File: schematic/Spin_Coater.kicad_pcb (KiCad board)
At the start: 2 copper layers, 135 x 80 mm, 97 parts, among them J1 USB_C_Receptacle_USB2.0_14P, J2 Motor Encoder In, J3 USB_B_Micro, M1A TestPoint, M1B TestPoint, M1C TestPoint, Q1 AONR21357, Q2 GSFN6982, Q3 GSFN6982, Q4 GSFN6982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

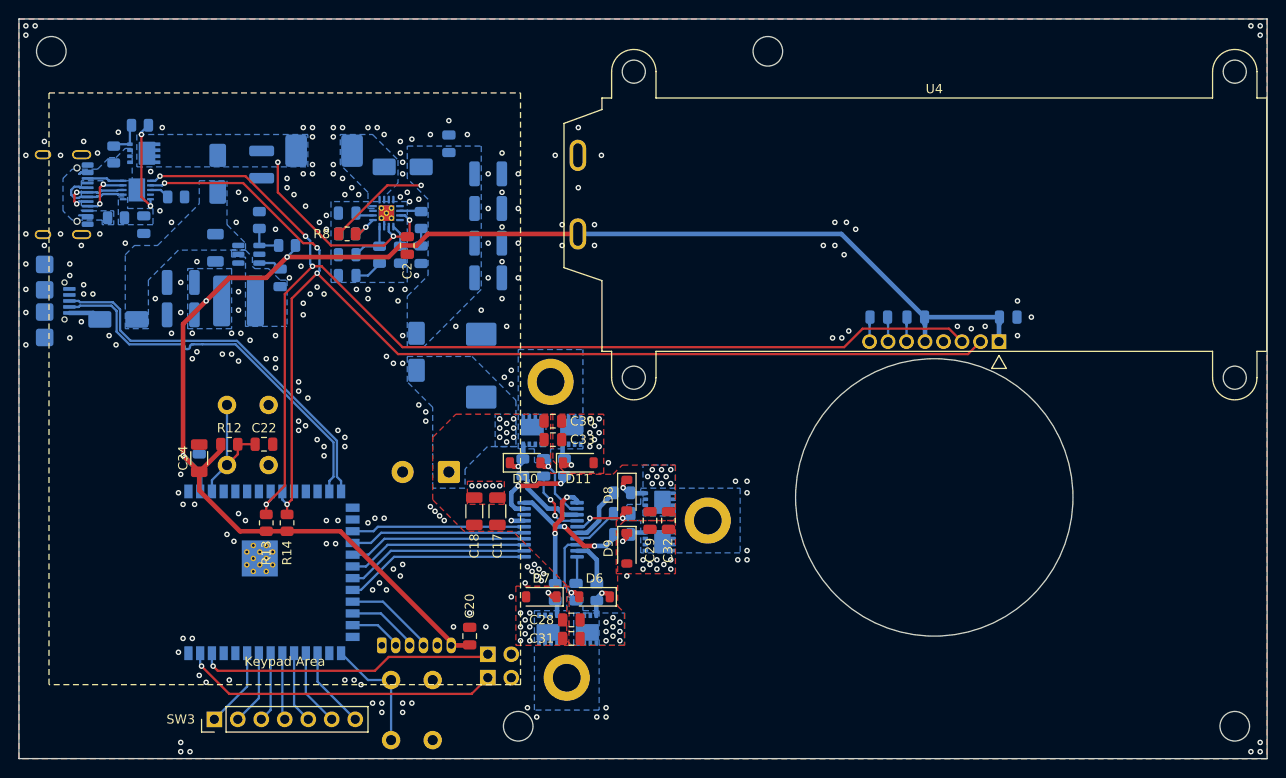
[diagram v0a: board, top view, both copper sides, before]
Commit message: Added button debouncing
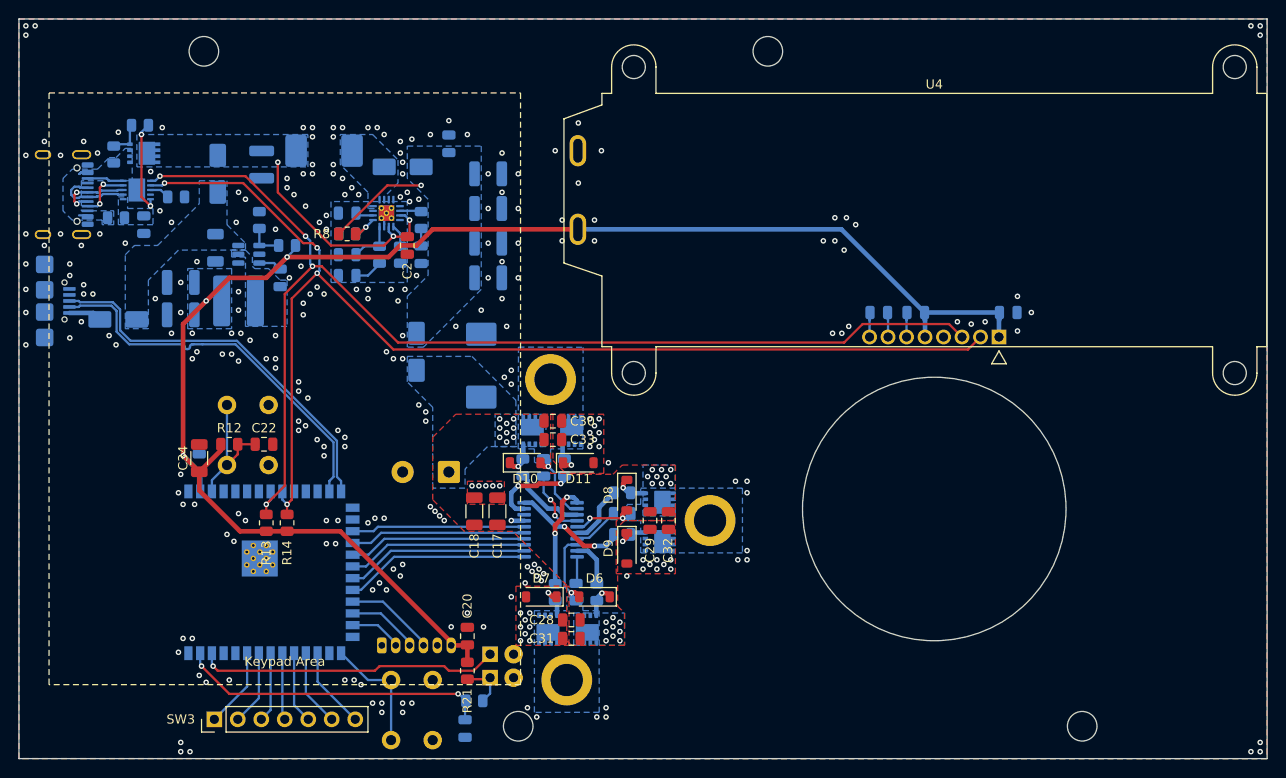
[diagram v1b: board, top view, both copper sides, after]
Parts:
- added C36: 1uF, Capacitor_SMD:C_0805_2012Metric, B.Cu at (120.8, 146.8)
- added R21: 10k, Resistor_SMD:R_0805_2012Metric, F.Cu at (121.0, 140.5)
- added R22: 10k, Resistor_SMD:R_0805_2012Metric, B.Cu at (121.8, 143.8)
- M1A, M1B, M1C: footprint footprints:TestPoint_THTPad_D5.0mm_Drill3.0mm -> footprints:TestPoint_THTPad_D5.5mm_Drill3.5mm
- moved H2 16.5 mm to (92.5, 73.5)
- moved H3 16.5 mm to (187.5, 146.5)
- moved C14 0.50 mm to (165.5, 101.8)
- moved C7 0.50 mm to (179.5, 101.8)
- moved C9 0.50 mm to (169.5, 101.8)
- moved G*** 0.50 mm to (162.5, 85.8)
- moved U4 0.50 mm to (171.5, 88.5)
- moved C20 0.25 mm to (121.0, 136.8)
- moved M1A 0.25 mm to (131.8, 141.5), turned to 0 degrees
- moved M1B 0.25 mm to (147.2, 124.2)
- moved M1C 0.25 mm to (130.0, 109.0)
- moved SW4 0.25 mm to (126.0, 141.2)
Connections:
- SW4 pad 2: /SW -> Net-(R21-Pad1)
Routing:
- net Net-(R21-Pad1): track 0.00 -> 5.11 mm
- net +3.3V: track 166.4 -> 168.6 mm
- net /LED: track 32.1 -> 32.9 mm
- net /SW: track 34.4 -> 33.7 mm, vias 1 -> 2
- net GND: vias 271 -> 270
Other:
- outline, holes or cut-outs redrawn

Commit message: Hopefully final revision
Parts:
- renumbered M1A to M1A1, M1B to M1B1, M1C to M1C1
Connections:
- U2 pad 9: GND -> unconnected-(U2-ISET-Pad9)
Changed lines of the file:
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@@
 		(descr "THT pad as test Point, diameter 5.0mm, hole diameter 3.0mm")
 		(tags "test point THT pad")
-		(property "Reference" "M1B"
+		(property "Reference" "M1B1"
 			(at 0 4 0)
 			(layer "B.SilkS")
@@
 			(layers "B.Cu" "B.Mask" "B.Paste")
 			(roundrect_rratio 0.25)
-			(net "GND")
+			(net "unconnected-(U2-ISET-Pad9)")
 			(pinfunction "ISET_9")
-			(pintype "input")
+			(pintype "input+no_connect")
 		)
 		(pad "10" smd roundrect
@@
 		(descr "THT pad as test Point, diameter 5.0mm, hole diameter 3.0mm")
 		(tags "test point THT pad")
-		(property "Reference" "M1C"
+		(property "Reference" "M1C1"
 			(at 0 4 0)
 			(layer "B.SilkS")
@@
 		(descr "THT pad as test Point, diameter 5.0mm, hole diameter 3.0mm")
 		(tags "test point THT pad")
-		(property "Reference" "M1A"
+		(property "Reference" "M1A1"
 			(at 0 4 180)
 			(layer "B.SilkS")
